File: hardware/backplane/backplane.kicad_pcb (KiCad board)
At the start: 4 copper layers, 123.4 x 458 mm, 31 parts, among them J1 Conn_02x34_Odd_Even, J101 Conn_02x34_Odd_Even, J102 ERF8-060-05.0-L-DV, J103 Conn_02x34_Odd_Even, J2 ERF8-060-05.0-L-DV, J201 Conn_02x34_Odd_Even-Connector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, J203 Conn_02x34_Odd_Even-Connector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, J3 Conn_02x34_Odd_Even, J301 Conn_02x34_Odd_Even-Connector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, J302 ERF8-060-05.0-L-DV, J303 Conn_02x34_Odd_Even-Connector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, J401 Conn_02x34_Odd_Even, J402 ERF8-060-05.0-L-DV, J403 Conn_02x34_Odd_Even, J501 Conn_02x34_Odd_Even-Connector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, J503 Conn_02x34_Odd_Even-Connector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, J601 Conn_02x34_Odd_Even-Connector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, J602 ERF8-060-05.0-L-DV, J603 Conn_02x34_Odd_Even-Connector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, J701 Conn_02x34_Odd_Even, J702 ERF8-060-05.0-L-DV, J703 Conn_02x34_Odd_Even, J801 Conn_02x34_Odd_Even-Connector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, J803 Conn_02x34_Odd_Even-Connector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, J901 Conn_02x34_Odd_Even-Connector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, J902 ERF8-060-05.0-L-DV, J903 Conn_02x34_Odd_Even-Connector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

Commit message: Backplane Layout in process
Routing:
- net GND: track 118.4 -> 530.2 mm, vias 42 -> 185
- net /SiPM_Connector(1-3)/BIAS1: track 0.00 -> 275.8 mm, vias 0 -> 5
- net /SiPM_Connector(1-3)/BIAS2: track 0.00 -> 111.6 mm, vias 0 -> 5
- net /SiPM_Connector(1-3)/OUT: track 0.00 -> 57.8 mm, vias 0 -> 3
- net /SiPM_Connector(1-3)/VDD: track 0.00 -> 54.1 mm, vias 0 -> 3
- net /SiPM_Connector(1-3)/BIAS3: track 0.00 -> 46.7 mm, vias 0 -> 1
- net /SiPM_Connector(1-3)/CH46: track 0.00 -> 40.6 mm, vias 0 -> 4
- net /SiPM_Connector(1-3)/CH45: track 0.00 -> 39.9 mm, vias 0 -> 2
- net /SiPM_Connector(1-3)/CH47: track 0.00 -> 39.7 mm, vias 0 -> 2
- net /SiPM_Connector(1-3)/CH53: track 0.00 -> 39.5 mm, vias 0 -> 2
- net /SiPM_Connector(1-3)/CH56: track 0.00 -> 39.4 mm, vias 0 -> 2
- net /SiPM_Connector(1-3)/CH52: track 0.00 -> 39.3 mm, vias 0 -> 4
- net /SiPM_Connector(1-3)/CH55: track 0.00 -> 39.2 mm, vias 0 -> 4
- net /SiPM_Connector(1-3)/CH54: track 0.00 -> 39.1 mm, vias 0 -> 2
- net /SiPM_Connector(1-3)/CH44: track 0.00 -> 39.0 mm, vias 0 -> 2
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
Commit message: Backplane layout in process
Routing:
- net /SiPM_Connector(1-3)/BIAS1: track 275.8 -> 161.3 mm, vias 5 -> 3
- net /SiPM_Connector(1-3)/BIAS3: track 46.7 -> 161.3 mm, vias 1 -> 3
- net GND: track 530.2 -> 476.0 mm, vias 185 -> 168
- net /SiPM_Connector(1-3)/BIAS4: track 15.9 -> 63.8 mm, vias 1 -> 3
- net /SiPM_Connector(1-3)/BIAS2: track 111.6 -> 63.8 mm, vias 5 -> 3
- net /SiPM_Connector(1-3)/BCH46: track 0.00 -> 20.3 mm, vias 0 -> 2
- net /SiPM_Connector(1-3)/CH46: track 40.6 -> 20.3 mm, vias 4 -> 2
- net /SiPM_Connector(1-3)/BCH45: track 0.00 -> 20.0 mm, vias 0 -> 1
- net /SiPM_Connector(1-3)/CH45: track 39.9 -> 20.0 mm, vias 2 -> 1
- net /SiPM_Connector(1-3)/CH47: track 39.7 -> 19.8 mm, vias 2 -> 1
- net /SiPM_Connector(1-3)/BCH47: track 0.00 -> 19.8 mm, vias 0 -> 1
- net /SiPM_Connector(1-3)/BCH53: track 0.00 -> 19.7 mm, vias 0 -> 1
- net /SiPM_Connector(1-3)/CH53: track 39.5 -> 19.7 mm, vias 2 -> 1
- net /SiPM_Connector(1-3)/BCH56: track 0.00 -> 19.7 mm, vias 0 -> 1
- net /SiPM_Connector(1-3)/CH56: track 39.4 -> 19.7 mm, vias 2 -> 1
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
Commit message: SiPM Board RevC layout modified
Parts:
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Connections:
- J103 pad 1: Net-(J103-Pad1) -> /SiPM_Connector(1-3)/BIAS3
- J103 pad 10: GND -> /SiPM_Connector(1-3)/BCH4
- J103 pad 11: /SiPM_Connector(1-3)/BCH28 -> GND
- J103 pad 12: GND -> /SiPM_Connector(1-3)/BCH5
- J103 pad 13: /SiPM_Connector(1-3)/BCH27 -> GND
- J103 pad 14: GND -> /SiPM_Connector(1-3)/BCH6
- J103 pad 15: /SiPM_Connector(1-3)/BCH26 -> GND
- J103 pad 16: GND -> /SiPM_Connector(1-3)/BCH7
- J103 pad 17: /SiPM_Connector(1-3)/BCH25 -> GND
- J103 pad 18: GND -> /SiPM_Connector(1-3)/BCH8
- J103 pad 19: /SiPM_Connector(1-3)/BCH24 -> GND
- J103 pad 2: /SiPM_Connector(1-3)/BIAS4 -> /SiPM_Connector(1-3)/BCH0
- J103 pad 20: GND -> /SiPM_Connector(1-3)/BCH9
- J103 pad 21: /SiPM_Connector(1-3)/BCH23 -> GND
- J103 pad 22: GND -> /SiPM_Connector(1-3)/BCH10
- J103 pad 23: /SiPM_Connector(1-3)/BCH22 -> GND
- J103 pad 24: GND -> /SiPM_Connector(1-3)/BCH11
- J103 pad 25: /SiPM_Connector(1-3)/BCH21 -> GND
- J103 pad 26: GND -> /SiPM_Connector(1-3)/BCH12
- J103 pad 27: /SiPM_Connector(1-3)/BCH20 -> GND
- J103 pad 28: GND -> /SiPM_Connector(1-3)/BCH13
- J103 pad 29: /SiPM_Connector(1-3)/BCH19 -> GND
- J103 pad 3: Net-(J103-Pad3) -> GND
- J103 pad 30: GND -> /SiPM_Connector(1-3)/BCH14
- J103 pad 31: /SiPM_Connector(1-3)/BCH18 -> GND
- J103 pad 32: GND -> /SiPM_Connector(1-3)/BCH15
- J103 pad 33: /SiPM_Connector(1-3)/BCH17 -> GND
- J103 pad 34: GND -> /SiPM_Connector(1-3)/BCH16
- J103 pad 35: /SiPM_Connector(1-3)/BCH16 -> GND
- J103 pad 36: GND -> /SiPM_Connector(1-3)/BCH17
- J103 pad 37: /SiPM_Connector(1-3)/BCH15 -> GND
- J103 pad 38: GND -> /SiPM_Connector(1-3)/BCH18
- J103 pad 39: /SiPM_Connector(1-3)/BCH14 -> GND
- J103 pad 4: GND -> /SiPM_Connector(1-3)/BCH1
- J103 pad 40: GND -> /SiPM_Connector(1-3)/BCH19
- J103 pad 41: /SiPM_Connector(1-3)/BCH13 -> GND
- J103 pad 42: GND -> /SiPM_Connector(1-3)/BCH20
- J103 pad 43: /SiPM_Connector(1-3)/BCH12 -> GND
- J103 pad 44: GND -> /SiPM_Connector(1-3)/BCH21
- J103 pad 45: /SiPM_Connector(1-3)/BCH11 -> GND
- J103 pad 46: GND -> /SiPM_Connector(1-3)/BCH22
- J103 pad 47: /SiPM_Connector(1-3)/BCH10 -> GND
- J103 pad 48: GND -> /SiPM_Connector(1-3)/BCH23
- J103 pad 49: /SiPM_Connector(1-3)/BCH9 -> GND
- J103 pad 5: /SiPM_Connector(1-3)/BCH31 -> GND
- J103 pad 50: GND -> /SiPM_Connector(1-3)/BCH24
- J103 pad 51: /SiPM_Connector(1-3)/BCH8 -> GND
- J103 pad 52: GND -> /SiPM_Connector(1-3)/BCH25
- J103 pad 53: /SiPM_Connector(1-3)/BCH7 -> GND
- J103 pad 54: GND -> /SiPM_Connector(1-3)/BCH26
- J103 pad 55: /SiPM_Connector(1-3)/BCH6 -> GND
- J103 pad 56: GND -> /SiPM_Connector(1-3)/BCH27
- J103 pad 57: /SiPM_Connector(1-3)/BCH5 -> GND
- J103 pad 58: GND -> /SiPM_Connector(1-3)/BCH28
- J103 pad 59: /SiPM_Connector(1-3)/BCH4 -> GND
- J103 pad 6: GND -> /SiPM_Connector(1-3)/BCH2
- J103 pad 60: GND -> /SiPM_Connector(1-3)/BCH29
- J103 pad 61: /SiPM_Connector(1-3)/BCH3 -> GND
- J103 pad 62: GND -> /SiPM_Connector(1-3)/BCH30
- J103 pad 63: /SiPM_Connector(1-3)/BCH2 -> GND
- J103 pad 64: GND -> /SiPM_Connector(1-3)/BCH31
- J103 pad 65: /SiPM_Connector(1-3)/BCH1 -> GND
- J103 pad 66: GND -> Net-(J103-Pad66)
- J103 pad 67: /SiPM_Connector(1-3)/BCH0 -> /SiPM_Connector(1-3)/BIAS4
- J103 pad 68: /SiPM_Connector(1-3)/BIAS3 -> Net-(J103-Pad68)
- J103 pad 7: /SiPM_Connector(1-3)/BCH30 -> GND
- J103 pad 8: GND -> /SiPM_Connector(1-3)/BCH3
- J103 pad 9: /SiPM_Connector(1-3)/BCH29 -> GND
- J203 pad 1: Net-(J203-Pad1) -> /SiPM_Connector(1-3)/BIAS3
- J203 pad 10: GND -> /SiPM_Connector(1-3)/BCH36
- J203 pad 11: /SiPM_Connector(1-3)/BCH60 -> GND
- J203 pad 12: GND -> /SiPM_Connector(1-3)/BCH37
- J203 pad 13: /SiPM_Connector(1-3)/BCH59 -> GND
- J203 pad 14: GND -> /SiPM_Connector(1-3)/BCH38
- J203 pad 15: /SiPM_Connector(1-3)/BCH58 -> GND
- J203 pad 16: GND -> /SiPM_Connector(1-3)/BCH39
- J203 pad 17: /SiPM_Connector(1-3)/BCH57 -> GND
- J203 pad 18: GND -> /SiPM_Connector(1-3)/BCH40
- J203 pad 19: /SiPM_Connector(1-3)/BCH56 -> GND
- J203 pad 2: /SiPM_Connector(1-3)/BIAS4 -> /SiPM_Connector(1-3)/BCH32
- J203 pad 20: GND -> /SiPM_Connector(1-3)/BCH41
- J203 pad 21: /SiPM_Connector(1-3)/BCH55 -> GND
- J203 pad 22: GND -> /SiPM_Connector(1-3)/BCH42
- J203 pad 23: /SiPM_Connector(1-3)/BCH54 -> GND
- J203 pad 24: GND -> /SiPM_Connector(1-3)/BCH43
- J203 pad 25: /SiPM_Connector(1-3)/BCH53 -> GND
- J203 pad 26: GND -> /SiPM_Connector(1-3)/BCH44
- J203 pad 27: /SiPM_Connector(1-3)/BCH52 -> GND
- J203 pad 28: GND -> /SiPM_Connector(1-3)/BCH45
- J203 pad 29: /SiPM_Connector(1-3)/BCH51 -> GND
- J203 pad 3: Net-(J203-Pad3) -> GND
- J203 pad 30: GND -> /SiPM_Connector(1-3)/BCH46
- J203 pad 31: /SiPM_Connector(1-3)/BCH50 -> GND
- J203 pad 32: GND -> /SiPM_Connector(1-3)/BCH47
- J203 pad 33: /SiPM_Connector(1-3)/BCH49 -> GND
- J203 pad 34: GND -> /SiPM_Connector(1-3)/BCH48
- J203 pad 35: /SiPM_Connector(1-3)/BCH48 -> GND
- J203 pad 36: GND -> /SiPM_Connector(1-3)/BCH49
- J203 pad 37: /SiPM_Connector(1-3)/BCH47 -> GND
- J203 pad 38: GND -> /SiPM_Connector(1-3)/BCH50
- J203 pad 39: /SiPM_Connector(1-3)/BCH46 -> GND
- J203 pad 4: GND -> /SiPM_Connector(1-3)/BCH33
- J203 pad 40: GND -> /SiPM_Connector(1-3)/BCH51
- J203 pad 41: /SiPM_Connector(1-3)/BCH45 -> GND
- J203 pad 42: GND -> /SiPM_Connector(1-3)/BCH52
- J203 pad 43: /SiPM_Connector(1-3)/BCH44 -> GND
- J203 pad 44: GND -> /SiPM_Connector(1-3)/BCH53
- J203 pad 45: /SiPM_Connector(1-3)/BCH43 -> GND
- J203 pad 46: GND -> /SiPM_Connector(1-3)/BCH54
- J203 pad 47: /SiPM_Connector(1-3)/BCH42 -> GND
- J203 pad 48: GND -> /SiPM_Connector(1-3)/BCH55
- J203 pad 49: /SiPM_Connector(1-3)/BCH41 -> GND
- J203 pad 5: /SiPM_Connector(1-3)/BCH63 -> GND
- J203 pad 50: GND -> /SiPM_Connector(1-3)/BCH56
- J203 pad 51: /SiPM_Connector(1-3)/BCH40 -> GND
- J203 pad 52: GND -> /SiPM_Connector(1-3)/BCH57
- J203 pad 53: /SiPM_Connector(1-3)/BCH39 -> GND
- J203 pad 54: GND -> /SiPM_Connector(1-3)/BCH58
- J203 pad 55: /SiPM_Connector(1-3)/BCH38 -> GND
- J203 pad 56: GND -> /SiPM_Connector(1-3)/BCH59
- J203 pad 57: /SiPM_Connector(1-3)/BCH37 -> GND
- J203 pad 58: GND -> /SiPM_Connector(1-3)/BCH60
- J203 pad 59: /SiPM_Connector(1-3)/BCH36 -> GND
- J203 pad 6: GND -> /SiPM_Connector(1-3)/BCH34
- J203 pad 60: GND -> /SiPM_Connector(1-3)/BCH61
- J203 pad 61: /SiPM_Connector(1-3)/BCH35 -> GND
- J203 pad 62: GND -> /SiPM_Connector(1-3)/BCH62
- J203 pad 63: /SiPM_Connector(1-3)/BCH34 -> GND
- J203 pad 64: GND -> /SiPM_Connector(1-3)/BCH63
- J203 pad 65: /SiPM_Connector(1-3)/BCH33 -> GND
- J203 pad 66: GND -> Net-(J203-Pad66)
- J203 pad 67: /SiPM_Connector(1-3)/BCH32 -> /SiPM_Connector(1-3)/BIAS4
- J203 pad 68: /SiPM_Connector(1-3)/BIAS3 -> Net-(J203-Pad68)
- J203 pad 7: /SiPM_Connector(1-3)/BCH62 -> GND
- J203 pad 8: GND -> /SiPM_Connector(1-3)/BCH35
- J203 pad 9: /SiPM_Connector(1-3)/BCH61 -> GND
- J303 pad 1: Net-(J303-Pad1) -> /SiPM_Connector(1-3)/BIAS3
- J303 pad 10: GND -> /SiPM_Connector(1-3)/BCH68
- J303 pad 11: /SiPM_Connector(1-3)/BCH92 -> GND
- J303 pad 12: GND -> /SiPM_Connector(1-3)/BCH69
- J303 pad 13: /SiPM_Connector(1-3)/BCH91 -> GND
- J303 pad 14: GND -> /SiPM_Connector(1-3)/BCH70
- J303 pad 15: /SiPM_Connector(1-3)/BCH90 -> GND
- J303 pad 16: GND -> /SiPM_Connector(1-3)/BCH71
- J303 pad 17: /SiPM_Connector(1-3)/BCH89 -> GND
- J303 pad 18: GND -> /SiPM_Connector(1-3)/BCH72
- J303 pad 19: /SiPM_Connector(1-3)/BCH88 -> GND
- J303 pad 2: /SiPM_Connector(1-3)/BIAS4 -> /SiPM_Connector(1-3)/BCH64
- J303 pad 20: GND -> /SiPM_Connector(1-3)/BCH73
- J303 pad 21: /SiPM_Connector(1-3)/BCH87 -> GND
- J303 pad 22: GND -> /SiPM_Connector(1-3)/BCH74
- J303 pad 23: /SiPM_Connector(1-3)/BCH86 -> GND
- J303 pad 24: GND -> /SiPM_Connector(1-3)/BCH75
- J303 pad 25: /SiPM_Connector(1-3)/BCH85 -> GND
- J303 pad 26: GND -> /SiPM_Connector(1-3)/BCH76
- J303 pad 27: /SiPM_Connector(1-3)/BCH84 -> GND
- J303 pad 28: GND -> /SiPM_Connector(1-3)/BCH77
- J303 pad 29: /SiPM_Connector(1-3)/BCH83 -> GND
- J303 pad 3: Net-(J303-Pad3) -> GND
- J303 pad 30: GND -> /SiPM_Connector(1-3)/BCH78
- J303 pad 31: /SiPM_Connector(1-3)/BCH82 -> GND
- J303 pad 32: GND -> /SiPM_Connector(1-3)/BCH79
- J303 pad 33: /SiPM_Connector(1-3)/BCH81 -> GND
- J303 pad 34: GND -> /SiPM_Connector(1-3)/BCH80
- J303 pad 35: /SiPM_Connector(1-3)/BCH80 -> GND
- J303 pad 36: GND -> /SiPM_Connector(1-3)/BCH81
- J303 pad 37: /SiPM_Connector(1-3)/BCH79 -> GND
- J303 pad 38: GND -> /SiPM_Connector(1-3)/BCH82
- J303 pad 39: /SiPM_Connector(1-3)/BCH78 -> GND
- J303 pad 4: GND -> /SiPM_Connector(1-3)/BCH65
- J303 pad 40: GND -> /SiPM_Connector(1-3)/BCH83
- J303 pad 41: /SiPM_Connector(1-3)/BCH77 -> GND
- J303 pad 42: GND -> /SiPM_Connector(1-3)/BCH84
- J303 pad 43: /SiPM_Connector(1-3)/BCH76 -> GND
- J303 pad 44: GND -> /SiPM_Connector(1-3)/BCH85
- J303 pad 45: /SiPM_Connector(1-3)/BCH75 -> GND
- J303 pad 46: GND -> /SiPM_Connector(1-3)/BCH86
- J303 pad 47: /SiPM_Connector(1-3)/BCH74 -> GND
- J303 pad 48: GND -> /SiPM_Connector(1-3)/BCH87
- J303 pad 49: /SiPM_Connector(1-3)/BCH73 -> GND
- J303 pad 5: /SiPM_Connector(1-3)/BCH95 -> GND
- J303 pad 50: GND -> /SiPM_Connector(1-3)/BCH88
- J303 pad 51: /SiPM_Connector(1-3)/BCH72 -> GND
- J303 pad 52: GND -> /SiPM_Connector(1-3)/BCH89
- J303 pad 53: /SiPM_Connector(1-3)/BCH71 -> GND
- J303 pad 54: GND -> /SiPM_Connector(1-3)/BCH90
- J303 pad 55: /SiPM_Connector(1-3)/BCH70 -> GND
- J303 pad 56: GND -> /SiPM_Connector(1-3)/BCH91
- J303 pad 57: /SiPM_Connector(1-3)/BCH69 -> GND
- J303 pad 58: GND -> /SiPM_Connector(1-3)/BCH92
- J303 pad 59: /SiPM_Connector(1-3)/BCH68 -> GND
- J303 pad 6: GND -> /SiPM_Connector(1-3)/BCH66
- J303 pad 60: GND -> /SiPM_Connector(1-3)/BCH93
- J303 pad 61: /SiPM_Connector(1-3)/BCH67 -> GND
- J303 pad 62: GND -> /SiPM_Connector(1-3)/BCH94
- J303 pad 63: /SiPM_Connector(1-3)/BCH66 -> GND
- J303 pad 64: GND -> /SiPM_Connector(1-3)/BCH95
- J303 pad 65: /SiPM_Connector(1-3)/BCH65 -> GND
- J303 pad 66: GND -> Net-(J303-Pad66)
- J303 pad 67: /SiPM_Connector(1-3)/BCH64 -> /SiPM_Connector(1-3)/BIAS4
- J303 pad 68: /SiPM_Connector(1-3)/BIAS3 -> Net-(J303-Pad68)
- J303 pad 7: /SiPM_Connector(1-3)/BCH94 -> GND
- J303 pad 8: GND -> /SiPM_Connector(1-3)/BCH67
- J303 pad 9: /SiPM_Connector(1-3)/BCH93 -> GND
- J403 pad 1: Net-(J403-Pad1) -> /SiPM_Connector(4-6)/BIAS3
- J403 pad 10: GND -> /SiPM_Connector(4-6)/BCH4
- J403 pad 11: /SiPM_Connector(4-6)/BCH28 -> GND
- J403 pad 12: GND -> /SiPM_Connector(4-6)/BCH5
- J403 pad 13: /SiPM_Connector(4-6)/BCH27 -> GND
- J403 pad 14: GND -> /SiPM_Connector(4-6)/BCH6
- J403 pad 15: /SiPM_Connector(4-6)/BCH26 -> GND
- J403 pad 16: GND -> /SiPM_Connector(4-6)/BCH7
- J403 pad 17: /SiPM_Connector(4-6)/BCH25 -> GND
- J403 pad 18: GND -> /SiPM_Connector(4-6)/BCH8
- J403 pad 19: /SiPM_Connector(4-6)/BCH24 -> GND
- J403 pad 2: /SiPM_Connector(4-6)/BIAS4 -> /SiPM_Connector(4-6)/BCH0
- J403 pad 20: GND -> /SiPM_Connector(4-6)/BCH9
- J403 pad 21: /SiPM_Connector(4-6)/BCH23 -> GND
- J403 pad 22: GND -> /SiPM_Connector(4-6)/BCH10
- J403 pad 23: /SiPM_Connector(4-6)/BCH22 -> GND
- J403 pad 24: GND -> /SiPM_Connector(4-6)/BCH11
- J403 pad 25: /SiPM_Connector(4-6)/BCH21 -> GND
- J403 pad 26: GND -> /SiPM_Connector(4-6)/BCH12
- J403 pad 27: /SiPM_Connector(4-6)/BCH20 -> GND
- J403 pad 28: GND -> /SiPM_Connector(4-6)/BCH13
- J403 pad 29: /SiPM_Connector(4-6)/BCH19 -> GND
- J403 pad 3: Net-(J403-Pad3) -> GND
- J403 pad 30: GND -> /SiPM_Connector(4-6)/BCH14
- J403 pad 31: /SiPM_Connector(4-6)/BCH18 -> GND
- J403 pad 32: GND -> /SiPM_Connector(4-6)/BCH15
- J403 pad 33: /SiPM_Connector(4-6)/BCH17 -> GND
- J403 pad 34: GND -> /SiPM_Connector(4-6)/BCH16
- J403 pad 35: /SiPM_Connector(4-6)/BCH16 -> GND
- J403 pad 36: GND -> /SiPM_Connector(4-6)/BCH17
- J403 pad 37: /SiPM_Connector(4-6)/BCH15 -> GND
- J403 pad 38: GND -> /SiPM_Connector(4-6)/BCH18
- J403 pad 39: /SiPM_Connector(4-6)/BCH14 -> GND
- J403 pad 4: GND -> /SiPM_Connector(4-6)/BCH1
- J403 pad 40: GND -> /SiPM_Connector(4-6)/BCH19
- J403 pad 41: /SiPM_Connector(4-6)/BCH13 -> GND
- J403 pad 42: GND -> /SiPM_Connector(4-6)/BCH20
- J403 pad 43: /SiPM_Connector(4-6)/BCH12 -> GND
- J403 pad 44: GND -> /SiPM_Connector(4-6)/BCH21
- J403 pad 45: /SiPM_Connector(4-6)/BCH11 -> GND
- J403 pad 46: GND -> /SiPM_Connector(4-6)/BCH22
- J403 pad 47: /SiPM_Connector(4-6)/BCH10 -> GND
- J403 pad 48: GND -> /SiPM_Connector(4-6)/BCH23
- J403 pad 49: /SiPM_Connector(4-6)/BCH9 -> GND
- J403 pad 5: /SiPM_Connector(4-6)/BCH31 -> GND
- J403 pad 50: GND -> /SiPM_Connector(4-6)/BCH24
- J403 pad 51: /SiPM_Connector(4-6)/BCH8 -> GND
- J403 pad 52: GND -> /SiPM_Connector(4-6)/BCH25
- J403 pad 53: /SiPM_Connector(4-6)/BCH7 -> GND
- J403 pad 54: GND -> /SiPM_Connector(4-6)/BCH26
- J403 pad 55: /SiPM_Connector(4-6)/BCH6 -> GND
- J403 pad 56: GND -> /SiPM_Connector(4-6)/BCH27
- J403 pad 57: /SiPM_Connector(4-6)/BCH5 -> GND
- J403 pad 58: GND -> /SiPM_Connector(4-6)/BCH28
- J403 pad 59: /SiPM_Connector(4-6)/BCH4 -> GND
- J403 pad 6: GND -> /SiPM_Connector(4-6)/BCH2
- J403 pad 60: GND -> /SiPM_Connector(4-6)/BCH29
- J403 pad 61: /SiPM_Connector(4-6)/BCH3 -> GND
- J403 pad 62: GND -> /SiPM_Connector(4-6)/BCH30
- J403 pad 63: /SiPM_Connector(4-6)/BCH2 -> GND
- J403 pad 64: GND -> /SiPM_Connector(4-6)/BCH31
- J403 pad 65: /SiPM_Connector(4-6)/BCH1 -> GND
- J403 pad 66: GND -> Net-(J403-Pad66)
- J403 pad 67: /SiPM_Connector(4-6)/BCH0 -> /SiPM_Connector(4-6)/BIAS4
- J403 pad 68: /SiPM_Connector(4-6)/BIAS3 -> Net-(J403-Pad68)
- J403 pad 7: /SiPM_Connector(4-6)/BCH30 -> GND
- J403 pad 8: GND -> /SiPM_Connector(4-6)/BCH3
- J403 pad 9: /SiPM_Connector(4-6)/BCH29 -> GND
- J503 pad 1: Net-(J503-Pad1) -> /SiPM_Connector(4-6)/BIAS3
- J503 pad 10: GND -> /SiPM_Connector(4-6)/BCH36
- J503 pad 11: /SiPM_Connector(4-6)/BCH60 -> GND
- J503 pad 12: GND -> /SiPM_Connector(4-6)/BCH37
- J503 pad 13: /SiPM_Connector(4-6)/BCH59 -> GND
- J503 pad 14: GND -> /SiPM_Connector(4-6)/BCH38
- J503 pad 15: /SiPM_Connector(4-6)/BCH58 -> GND
- J503 pad 16: GND -> /SiPM_Connector(4-6)/BCH39
- J503 pad 17: /SiPM_Connector(4-6)/BCH57 -> GND
- J503 pad 18: GND -> /SiPM_Connector(4-6)/BCH40
- J503 pad 19: /SiPM_Connector(4-6)/BCH56 -> GND
- J503 pad 2: /SiPM_Connector(4-6)/BIAS4 -> /SiPM_Connector(4-6)/BCH32
- J503 pad 20: GND -> /SiPM_Connector(4-6)/BCH41
- J503 pad 21: /SiPM_Connector(4-6)/BCH55 -> GND
- J503 pad 22: GND -> /SiPM_Connector(4-6)/BCH42
- J503 pad 23: /SiPM_Connector(4-6)/BCH54 -> GND
- J503 pad 24: GND -> /SiPM_Connector(4-6)/BCH43
- J503 pad 25: /SiPM_Connector(4-6)/BCH53 -> GND
- J503 pad 26: GND -> /SiPM_Connector(4-6)/BCH44
- J503 pad 27: /SiPM_Connector(4-6)/BCH52 -> GND
- J503 pad 28: GND -> /SiPM_Connector(4-6)/BCH45
- J503 pad 29: /SiPM_Connector(4-6)/BCH51 -> GND
- J503 pad 3: Net-(J503-Pad3) -> GND
- J503 pad 30: GND -> /SiPM_Connector(4-6)/BCH46
- J503 pad 31: /SiPM_Connector(4-6)/BCH50 -> GND
- J503 pad 32: GND -> /SiPM_Connector(4-6)/BCH47
- J503 pad 33: /SiPM_Connector(4-6)/BCH49 -> GND
- J503 pad 34: GND -> /SiPM_Connector(4-6)/BCH48
- J503 pad 35: /SiPM_Connector(4-6)/BCH48 -> GND
- J503 pad 36: GND -> /SiPM_Connector(4-6)/BCH49
- J503 pad 37: /SiPM_Connector(4-6)/BCH47 -> GND
- J503 pad 38: GND -> /SiPM_Connector(4-6)/BCH50
- J503 pad 39: /SiPM_Connector(4-6)/BCH46 -> GND
- J503 pad 4: GND -> /SiPM_Connector(4-6)/BCH33
- J503 pad 40: GND -> /SiPM_Connector(4-6)/BCH51
- J503 pad 41: /SiPM_Connector(4-6)/BCH45 -> GND
- J503 pad 42: GND -> /SiPM_Connector(4-6)/BCH52
- J503 pad 43: /SiPM_Connector(4-6)/BCH44 -> GND
- J503 pad 44: GND -> /SiPM_Connector(4-6)/BCH53
- J503 pad 45: /SiPM_Connector(4-6)/BCH43 -> GND
- J503 pad 46: GND -> /SiPM_Connector(4-6)/BCH54
- J503 pad 47: /SiPM_Connector(4-6)/BCH42 -> GND
- J503 pad 48: GND -> /SiPM_Connector(4-6)/BCH55
- J503 pad 49: /SiPM_Connector(4-6)/BCH41 -> GND
- J503 pad 5: /SiPM_Connector(4-6)/BCH63 -> GND
- J503 pad 50: GND -> /SiPM_Connector(4-6)/BCH56
- J503 pad 51: /SiPM_Connector(4-6)/BCH40 -> GND
- J503 pad 52: GND -> /SiPM_Connector(4-6)/BCH57
- J503 pad 53: /SiPM_Connector(4-6)/BCH39 -> GND
- J503 pad 54: GND -> /SiPM_Connector(4-6)/BCH58
- J503 pad 55: /SiPM_Connector(4-6)/BCH38 -> GND
- J503 pad 56: GND -> /SiPM_Connector(4-6)/BCH59
- J503 pad 57: /SiPM_Connector(4-6)/BCH37 -> GND
- J503 pad 58: GND -> /SiPM_Connector(4-6)/BCH60
- J503 pad 59: /SiPM_Connector(4-6)/BCH36 -> GND
- J503 pad 6: GND -> /SiPM_Connector(4-6)/BCH34
- J503 pad 60: GND -> /SiPM_Connector(4-6)/BCH61
- J503 pad 61: /SiPM_Connector(4-6)/BCH35 -> GND
- J503 pad 62: GND -> /SiPM_Connector(4-6)/BCH62
- J503 pad 63: /SiPM_Connector(4-6)/BCH34 -> GND
- J503 pad 64: GND -> /SiPM_Connector(4-6)/BCH63
- J503 pad 65: /SiPM_Connector(4-6)/BCH33 -> GND
- J503 pad 66: GND -> Net-(J503-Pad66)
- J503 pad 67: /SiPM_Connector(4-6)/BCH32 -> /SiPM_Connector(4-6)/BIAS4
- J503 pad 68: /SiPM_Connector(4-6)/BIAS3 -> Net-(J503-Pad68)
- J503 pad 7: /SiPM_Connector(4-6)/BCH62 -> GND
- J503 pad 8: GND -> /SiPM_Connector(4-6)/BCH35
- J503 pad 9: /SiPM_Connector(4-6)/BCH61 -> GND
- J603 pad 1: Net-(J603-Pad1) -> /SiPM_Connector(4-6)/BIAS3
- J603 pad 10: GND -> /SiPM_Connector(4-6)/BCH68
- J603 pad 11: /SiPM_Connector(4-6)/BCH92 -> GND
- J603 pad 12: GND -> /SiPM_Connector(4-6)/BCH69
- J603 pad 13: /SiPM_Connector(4-6)/BCH91 -> GND
- J603 pad 14: GND -> /SiPM_Connector(4-6)/BCH70
- J603 pad 15: /SiPM_Connector(4-6)/BCH90 -> GND
- J603 pad 16: GND -> /SiPM_Connector(4-6)/BCH71
- J603 pad 17: /SiPM_Connector(4-6)/BCH89 -> GND
- J603 pad 18: GND -> /SiPM_Connector(4-6)/BCH72
- J603 pad 19: /SiPM_Connector(4-6)/BCH88 -> GND
- J603 pad 2: /SiPM_Connector(4-6)/BIAS4 -> /SiPM_Connector(4-6)/BCH64
- J603 pad 20: GND -> /SiPM_Connector(4-6)/BCH73
- J603 pad 21: /SiPM_Connector(4-6)/BCH87 -> GND
- J603 pad 22: GND -> /SiPM_Connector(4-6)/BCH74
- J603 pad 23: /SiPM_Connector(4-6)/BCH86 -> GND
- J603 pad 24: GND -> /SiPM_Connector(4-6)/BCH75
- J603 pad 25: /SiPM_Connector(4-6)/BCH85 -> GND
- J603 pad 26: GND -> /SiPM_Connector(4-6)/BCH76
- J603 pad 27: /SiPM_Connector(4-6)/BCH84 -> GND
- J603 pad 28: GND -> /SiPM_Connector(4-6)/BCH77
- J603 pad 29: /SiPM_Connector(4-6)/BCH83 -> GND
- J603 pad 3: Net-(J603-Pad3) -> GND
- J603 pad 30: GND -> /SiPM_Connector(4-6)/BCH78
- J603 pad 31: /SiPM_Connector(4-6)/BCH82 -> GND
- J603 pad 32: GND -> /SiPM_Connector(4-6)/BCH79
- J603 pad 33: /SiPM_Connector(4-6)/BCH81 -> GND
- J603 pad 34: GND -> /SiPM_Connector(4-6)/BCH80
- J603 pad 35: /SiPM_Connector(4-6)/BCH80 -> GND
- J603 pad 36: GND -> /SiPM_Connector(4-6)/BCH81
- J603 pad 37: /SiPM_Connector(4-6)/BCH79 -> GND
- J603 pad 38: GND -> /SiPM_Connector(4-6)/BCH82
- J603 pad 39: /SiPM_Connector(4-6)/BCH78 -> GND
- J603 pad 4: GND -> /SiPM_Connector(4-6)/BCH65
- J603 pad 40: GND -> /SiPM_Connector(4-6)/BCH83
- J603 pad 41: /SiPM_Connector(4-6)/BCH77 -> GND
- J603 pad 42: GND -> /SiPM_Connector(4-6)/BCH84
- J603 pad 43: /SiPM_Connector(4-6)/BCH76 -> GND
- J603 pad 44: GND -> /SiPM_Connector(4-6)/BCH85
- J603 pad 45: /SiPM_Connector(4-6)/BCH75 -> GND
- J603 pad 46: GND -> /SiPM_Connector(4-6)/BCH86
- J603 pad 47: /SiPM_Connector(4-6)/BCH74 -> GND
- J603 pad 48: GND -> /SiPM_Connector(4-6)/BCH87
- J603 pad 49: /SiPM_Connector(4-6)/BCH73 -> GND
- J603 pad 5: /SiPM_Connector(4-6)/BCH95 -> GND
- J603 pad 50: GND -> /SiPM_Connector(4-6)/BCH88
- J603 pad 51: /SiPM_Connector(4-6)/BCH72 -> GND
- J603 pad 52: GND -> /SiPM_Connector(4-6)/BCH89
- J603 pad 53: /SiPM_Connector(4-6)/BCH71 -> GND
- J603 pad 54: GND -> /SiPM_Connector(4-6)/BCH90
- J603 pad 55: /SiPM_Connector(4-6)/BCH70 -> GND
- J603 pad 56: GND -> /SiPM_Connector(4-6)/BCH91
- J603 pad 57: /SiPM_Connector(4-6)/BCH69 -> GND
- J603 pad 58: GND -> /SiPM_Connector(4-6)/BCH92
- J603 pad 59: /SiPM_Connector(4-6)/BCH68 -> GND
- J603 pad 6: GND -> /SiPM_Connector(4-6)/BCH66
- J603 pad 60: GND -> /SiPM_Connector(4-6)/BCH93
- J603 pad 61: /SiPM_Connector(4-6)/BCH67 -> GND
- J603 pad 62: GND -> /SiPM_Connector(4-6)/BCH94
- J603 pad 63: /SiPM_Connector(4-6)/BCH66 -> GND
- J603 pad 64: GND -> /SiPM_Connector(4-6)/BCH95
- J603 pad 65: /SiPM_Connector(4-6)/BCH65 -> GND
- J603 pad 66: GND -> Net-(J603-Pad66)
- J603 pad 67: /SiPM_Connector(4-6)/BCH64 -> /SiPM_Connector(4-6)/BIAS4
- J603 pad 68: /SiPM_Connector(4-6)/BIAS3 -> Net-(J603-Pad68)
- J603 pad 7: /SiPM_Connector(4-6)/BCH94 -> GND
- J603 pad 8: GND -> /SiPM_Connector(4-6)/BCH67
- J603 pad 9: /SiPM_Connector(4-6)/BCH93 -> GND
- J703 pad 1: Net-(J703-Pad1) -> /SiPM_Connector(7-9)/BIAS3
- J703 pad 10: GND -> /SiPM_Connector(7-9)/BCH4
- J703 pad 11: /SiPM_Connector(7-9)/BCH28 -> GND
- J703 pad 12: GND -> /SiPM_Connector(7-9)/BCH5
- J703 pad 13: /SiPM_Connector(7-9)/BCH27 -> GND
- J703 pad 14: GND -> /SiPM_Connector(7-9)/BCH6
- J703 pad 15: /SiPM_Connector(7-9)/BCH26 -> GND
- J703 pad 16: GND -> /SiPM_Connector(7-9)/BCH7
- J703 pad 17: /SiPM_Connector(7-9)/BCH25 -> GND
- J703 pad 18: GND -> /SiPM_Connector(7-9)/BCH8
- J703 pad 19: /SiPM_Connector(7-9)/BCH24 -> GND
- J703 pad 2: /SiPM_Connector(7-9)/BIAS4 -> /SiPM_Connector(7-9)/BCH0
- J703 pad 20: GND -> /SiPM_Connector(7-9)/BCH9
- J703 pad 21: /SiPM_Connector(7-9)/BCH23 -> GND
- J703 pad 22: GND -> /SiPM_Connector(7-9)/BCH10
- J703 pad 23: /SiPM_Connector(7-9)/BCH22 -> GND
- J703 pad 24: GND -> /SiPM_Connector(7-9)/BCH11
- J703 pad 25: /SiPM_Connector(7-9)/BCH21 -> GND
- J703 pad 26: GND -> /SiPM_Connector(7-9)/BCH12
- J703 pad 27: /SiPM_Connector(7-9)/BCH20 -> GND
- J703 pad 28: GND -> /SiPM_Connector(7-9)/BCH13
- J703 pad 29: /SiPM_Connector(7-9)/BCH19 -> GND
- J703 pad 3: Net-(J703-Pad3) -> GND
- J703 pad 30: GND -> /SiPM_Connector(7-9)/BCH14
- J703 pad 31: /SiPM_Connector(7-9)/BCH18 -> GND
- J703 pad 32: GND -> /SiPM_Connector(7-9)/BCH15
- J703 pad 33: /SiPM_Connector(7-9)/BCH17 -> GND
- J703 pad 34: GND -> /SiPM_Connector(7-9)/BCH16
- J703 pad 35: /SiPM_Connector(7-9)/BCH16 -> GND
- J703 pad 36: GND -> /SiPM_Connector(7-9)/BCH17
- J703 pad 37: /SiPM_Connector(7-9)/BCH15 -> GND
- J703 pad 38: GND -> /SiPM_Connector(7-9)/BCH18
- J703 pad 39: /SiPM_Connector(7-9)/BCH14 -> GND
- J703 pad 4: GND -> /SiPM_Connector(7-9)/BCH1
- J703 pad 40: GND -> /SiPM_Connector(7-9)/BCH19
- J703 pad 41: /SiPM_Connector(7-9)/BCH13 -> GND
- J703 pad 42: GND -> /SiPM_Connector(7-9)/BCH20
- J703 pad 43: /SiPM_Connector(7-9)/BCH12 -> GND
- J703 pad 44: GND -> /SiPM_Connector(7-9)/BCH21
- J703 pad 45: /SiPM_Connector(7-9)/BCH11 -> GND
- J703 pad 46: GND -> /SiPM_Connector(7-9)/BCH22
- J703 pad 47: /SiPM_Connector(7-9)/BCH10 -> GND
- J703 pad 48: GND -> /SiPM_Connector(7-9)/BCH23
- J703 pad 49: /SiPM_Connector(7-9)/BCH9 -> GND
- J703 pad 5: /SiPM_Connector(7-9)/BCH31 -> GND
- J703 pad 50: GND -> /SiPM_Connector(7-9)/BCH24
- J703 pad 51: /SiPM_Connector(7-9)/BCH8 -> GND
- J703 pad 52: GND -> /SiPM_Connector(7-9)/BCH25
- J703 pad 53: /SiPM_Connector(7-9)/BCH7 -> GND
- J703 pad 54: GND -> /SiPM_Connector(7-9)/BCH26
- J703 pad 55: /SiPM_Connector(7-9)/BCH6 -> GND
- J703 pad 56: GND -> /SiPM_Connector(7-9)/BCH27
- J703 pad 57: /SiPM_Connector(7-9)/BCH5 -> GND
- J703 pad 58: GND -> /SiPM_Connector(7-9)/BCH28
- J703 pad 59: /SiPM_Connector(7-9)/BCH4 -> GND
- J703 pad 6: GND -> /SiPM_Connector(7-9)/BCH2
- J703 pad 60: GND -> /SiPM_Connector(7-9)/BCH29
- J703 pad 61: /SiPM_Connector(7-9)/BCH3 -> GND
- J703 pad 62: GND -> /SiPM_Connector(7-9)/BCH30
- J703 pad 63: /SiPM_Connector(7-9)/BCH2 -> GND
- J703 pad 64: GND -> /SiPM_Connector(7-9)/BCH31
- J703 pad 65: /SiPM_Connector(7-9)/BCH1 -> GND
- J703 pad 66: GND -> Net-(J703-Pad66)
- J703 pad 67: /SiPM_Connector(7-9)/BCH0 -> /SiPM_Connector(7-9)/BIAS4
- J703 pad 68: /SiPM_Connector(7-9)/BIAS3 -> Net-(J703-Pad68)
- J703 pad 7: /SiPM_Connector(7-9)/BCH30 -> GND
- J703 pad 8: GND -> /SiPM_Connector(7-9)/BCH3
- J703 pad 9: /SiPM_Connector(7-9)/BCH29 -> GND
- J803 pad 1: Net-(J803-Pad1) -> /SiPM_Connector(7-9)/BIAS3
- J803 pad 10: GND -> /SiPM_Connector(7-9)/BCH36
- J803 pad 11: /SiPM_Connector(7-9)/BCH60 -> GND
- J803 pad 12: GND -> /SiPM_Connector(7-9)/BCH37
- J803 pad 13: /SiPM_Connector(7-9)/BCH59 -> GND
- J803 pad 14: GND -> /SiPM_Connector(7-9)/BCH38
- J803 pad 15: /SiPM_Connector(7-9)/BCH58 -> GND
- J803 pad 16: GND -> /SiPM_Connector(7-9)/BCH39
- J803 pad 17: /SiPM_Connector(7-9)/BCH57 -> GND
- J803 pad 18: GND -> /SiPM_Connector(7-9)/BCH40
- J803 pad 19: /SiPM_Connector(7-9)/BCH56 -> GND
- J803 pad 2: /SiPM_Connector(7-9)/BIAS4 -> /SiPM_Connector(7-9)/BCH32
- J803 pad 20: GND -> /SiPM_Connector(7-9)/BCH41
- J803 pad 21: /SiPM_Connector(7-9)/BCH55 -> GND
- J803 pad 22: GND -> /SiPM_Connector(7-9)/BCH42
- J803 pad 23: /SiPM_Connector(7-9)/BCH54 -> GND
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
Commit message: Edited Backplane
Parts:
- moved J101 0.25 mm to (12.2, 25.0)
- moved J103 0.25 mm to (37.8, 25.0)
- moved J201 0.25 mm to (12.2, 76.0)
- moved J203 0.25 mm to (37.8, 76.0)
- moved J301 0.25 mm to (12.2, 127.0)
- moved J303 0.25 mm to (37.8, 127.0)
- moved J401 0.25 mm to (12.2, 178.0)
- moved J403 0.25 mm to (37.8, 178.0)
- moved J501 0.25 mm to (12.2, 229.0)
- moved J503 0.25 mm to (37.8, 229.0)
- moved J601 0.25 mm to (12.2, 280.0)
- moved J603 0.25 mm to (37.8, 280.0)
- moved J701 0.25 mm to (12.2, 331.0)
- moved J703 0.25 mm to (37.8, 331.0)
- moved J801 0.25 mm to (12.2, 382.0)
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- renumbered J702 to J1, J902 to J2
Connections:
- J1 pad 75: /SiPM_Connector(7-9)/BIAS3 -> /SiPM_Connector(7-9)/BIAS27
- J1 pad 76: /SiPM_Connector(7-9)/BIAS1 -> /SiPM_Connector(7-9)/BIAS25
- J1 pad 79: /SiPM_Connector(7-9)/BIAS4 -> /SiPM_Connector(7-9)/BIAS28
- J1 pad 80: /SiPM_Connector(7-9)/BIAS2 -> /SiPM_Connector(7-9)/BIAS26
- J2 pad 115: /SiPM_Connector(7-9)/BIAS3 -> /SiPM_Connector(7-9)/BIAS35
- J2 pad 116: /SiPM_Connector(7-9)/BIAS1 -> /SiPM_Connector(7-9)/BIAS33
- J2 pad 119: /SiPM_Connector(7-9)/BIAS4 -> /SiPM_Connector(7-9)/BIAS36
- J2 pad 120: /SiPM_Connector(7-9)/BIAS2 -> /SiPM_Connector(7-9)/BIAS34
- J2 pad 35: /SiPM_Connector(7-9)/BIAS3 -> /SiPM_Connector(7-9)/BIAS31
- J2 pad 36: /SiPM_Connector(7-9)/BIAS1 -> /SiPM_Connector(7-9)/BIAS29
- J2 pad 39: /SiPM_Connector(7-9)/BIAS4 -> /SiPM_Connector(7-9)/BIAS32
- J2 pad 40: /SiPM_Connector(7-9)/BIAS2 -> /SiPM_Connector(7-9)/BIAS30
- J201 pad 2: /SiPM_Connector(1-3)/BIAS1 -> /SiPM_Connector(1-3)/BIAS5
- J201 pad 68: /SiPM_Connector(1-3)/BIAS2 -> /SiPM_Connector(1-3)/BIAS6
- J203 pad 1: /SiPM_Connector(1-3)/BIAS3 -> /SiPM_Connector(1-3)/BIAS7
- J203 pad 67: /SiPM_Connector(1-3)/BIAS4 -> /SiPM_Connector(1-3)/BIAS8
- J301 pad 2: /SiPM_Connector(1-3)/BIAS1 -> /SiPM_Connector(1-3)/BIAS9
- J301 pad 68: /SiPM_Connector(1-3)/BIAS2 -> /SiPM_Connector(1-3)/BIAS10
- J302 pad 115: /SiPM_Connector(1-3)/BIAS3 -> /SiPM_Connector(1-3)/BIAS11
- J302 pad 116: /SiPM_Connector(1-3)/BIAS1 -> /SiPM_Connector(1-3)/BIAS9
- J302 pad 119: /SiPM_Connector(1-3)/BIAS4 -> /SiPM_Connector(1-3)/BIAS12
- J302 pad 120: /SiPM_Connector(1-3)/BIAS2 -> /SiPM_Connector(1-3)/BIAS10
- J302 pad 35: /SiPM_Connector(1-3)/BIAS3 -> /SiPM_Connector(1-3)/BIAS7
- J302 pad 36: /SiPM_Connector(1-3)/BIAS1 -> /SiPM_Connector(1-3)/BIAS5
- J302 pad 39: /SiPM_Connector(1-3)/BIAS4 -> /SiPM_Connector(1-3)/BIAS8
- J302 pad 40: /SiPM_Connector(1-3)/BIAS2 -> /SiPM_Connector(1-3)/BIAS6
- J303 pad 1: /SiPM_Connector(1-3)/BIAS3 -> /SiPM_Connector(1-3)/BIAS11
- J303 pad 67: /SiPM_Connector(1-3)/BIAS4 -> /SiPM_Connector(1-3)/BIAS12
- J401 pad 2: /SiPM_Connector(4-6)/BIAS1 -> /SiPM_Connector(4-6)/BIAS13
- J401 pad 68: /SiPM_Connector(4-6)/BIAS2 -> /SiPM_Connector(4-6)/BIAS14
- J402 pad 75: /SiPM_Connector(4-6)/BIAS3 -> /SiPM_Connector(4-6)/BIAS15
- J402 pad 76: /SiPM_Connector(4-6)/BIAS1 -> /SiPM_Connector(4-6)/BIAS13
- J402 pad 79: /SiPM_Connector(4-6)/BIAS4 -> /SiPM_Connector(4-6)/BIAS16
- J402 pad 80: /SiPM_Connector(4-6)/BIAS2 -> /SiPM_Connector(4-6)/BIAS14
- J403 pad 1: /SiPM_Connector(4-6)/BIAS3 -> /SiPM_Connector(4-6)/BIAS15
- J403 pad 67: /SiPM_Connector(4-6)/BIAS4 -> /SiPM_Connector(4-6)/BIAS16
- J501 pad 2: /SiPM_Connector(4-6)/BIAS1 -> /SiPM_Connector(4-6)/BIAS17
- J501 pad 68: /SiPM_Connector(4-6)/BIAS2 -> /SiPM_Connector(4-6)/BIAS18
- J503 pad 1: /SiPM_Connector(4-6)/BIAS3 -> /SiPM_Connector(4-6)/BIAS19
- J503 pad 67: /SiPM_Connector(4-6)/BIAS4 -> /SiPM_Connector(4-6)/BIAS20
- J601 pad 2: /SiPM_Connector(4-6)/BIAS1 -> /SiPM_Connector(4-6)/BIAS21
- J601 pad 68: /SiPM_Connector(4-6)/BIAS2 -> /SiPM_Connector(4-6)/BIAS22
- J602 pad 115: /SiPM_Connector(4-6)/BIAS3 -> /SiPM_Connector(4-6)/BIAS23
- J602 pad 116: /SiPM_Connector(4-6)/BIAS1 -> /SiPM_Connector(4-6)/BIAS21
- J602 pad 119: /SiPM_Connector(4-6)/BIAS4 -> /SiPM_Connector(4-6)/BIAS24
- J602 pad 120: /SiPM_Connector(4-6)/BIAS2 -> /SiPM_Connector(4-6)/BIAS22
- J602 pad 35: /SiPM_Connector(4-6)/BIAS3 -> /SiPM_Connector(4-6)/BIAS19
- J602 pad 36: /SiPM_Connector(4-6)/BIAS1 -> /SiPM_Connector(4-6)/BIAS17
- J602 pad 39: /SiPM_Connector(4-6)/BIAS4 -> /SiPM_Connector(4-6)/BIAS20
- J602 pad 40: /SiPM_Connector(4-6)/BIAS2 -> /SiPM_Connector(4-6)/BIAS18
- J603 pad 1: /SiPM_Connector(4-6)/BIAS3 -> /SiPM_Connector(4-6)/BIAS23
- J603 pad 67: /SiPM_Connector(4-6)/BIAS4 -> /SiPM_Connector(4-6)/BIAS24
- J701 pad 2: /SiPM_Connector(7-9)/BIAS1 -> /SiPM_Connector(7-9)/BIAS25
- J701 pad 68: /SiPM_Connector(7-9)/BIAS2 -> /SiPM_Connector(7-9)/BIAS26
- J703 pad 1: /SiPM_Connector(7-9)/BIAS3 -> /SiPM_Connector(7-9)/BIAS27
- J703 pad 67: /SiPM_Connector(7-9)/BIAS4 -> /SiPM_Connector(7-9)/BIAS28
- J801 pad 2: /SiPM_Connector(7-9)/BIAS1 -> /SiPM_Connector(7-9)/BIAS29
- J801 pad 68: /SiPM_Connector(7-9)/BIAS2 -> /SiPM_Connector(7-9)/BIAS30
- J803 pad 1: /SiPM_Connector(7-9)/BIAS3 -> /SiPM_Connector(7-9)/BIAS31
- J803 pad 67: /SiPM_Connector(7-9)/BIAS4 -> /SiPM_Connector(7-9)/BIAS32
- J901 pad 2: /SiPM_Connector(7-9)/BIAS1 -> /SiPM_Connector(7-9)/BIAS33
- J901 pad 68: /SiPM_Connector(7-9)/BIAS2 -> /SiPM_Connector(7-9)/BIAS34
- J903 pad 1: /SiPM_Connector(7-9)/BIAS3 -> /SiPM_Connector(7-9)/BIAS35
- J903 pad 67: /SiPM_Connector(7-9)/BIAS4 -> /SiPM_Connector(7-9)/BIAS36
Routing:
- net /SiPM_Connector(1-3)/BIAS1: track 161.3 -> 46.7 mm, vias 3 -> 1
- net /SiPM_Connector(1-3)/BIAS3: track 161.3 -> 46.7 mm, vias 3 -> 1
- net /SiPM_Connector(1-3)/BIAS7: track 0.00 -> 61.5 mm, vias 0 -> 1
- net /SiPM_Connector(1-3)/BIAS5: track 0.00 -> 61.5 mm, vias 0 -> 1
- net /SiPM_Connector(1-3)/BIAS11: track 0.00 -> 53.0 mm, vias 0 -> 1
- net /SiPM_Connector(1-3)/BIAS9: track 0.00 -> 53.0 mm, vias 0 -> 1
- net /SiPM_Connector(1-3)/BIAS4: track 63.8 -> 15.9 mm, vias 3 -> 1
- net /SiPM_Connector(1-3)/BIAS2: track 63.8 -> 15.9 mm, vias 3 -> 1
- net /SiPM_Connector(1-3)/BIAS6: track 0.00 -> 25.2 mm, vias 0 -> 1
- net /SiPM_Connector(1-3)/BIAS8: track 0.00 -> 25.2 mm, vias 0 -> 1
- net /SiPM_Connector(1-3)/BIAS12: track 0.00 -> 22.7 mm, vias 0 -> 1
- net /SiPM_Connector(1-3)/BIAS10: track 0.00 -> 22.7 mm, vias 0 -> 1

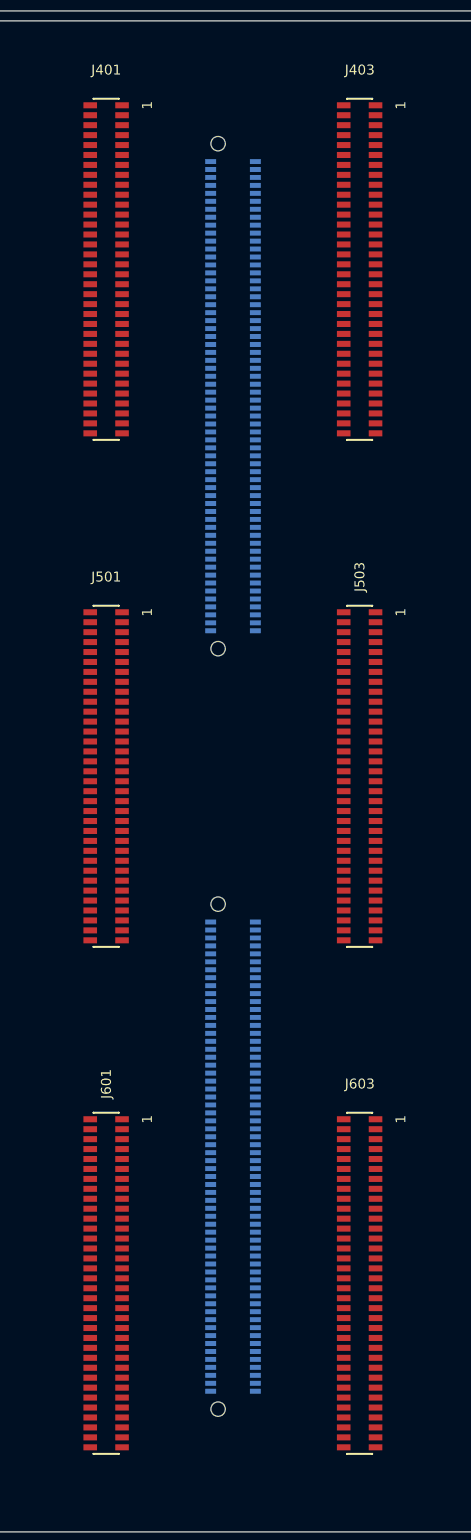
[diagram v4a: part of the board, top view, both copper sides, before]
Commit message: Backplane Layout edited
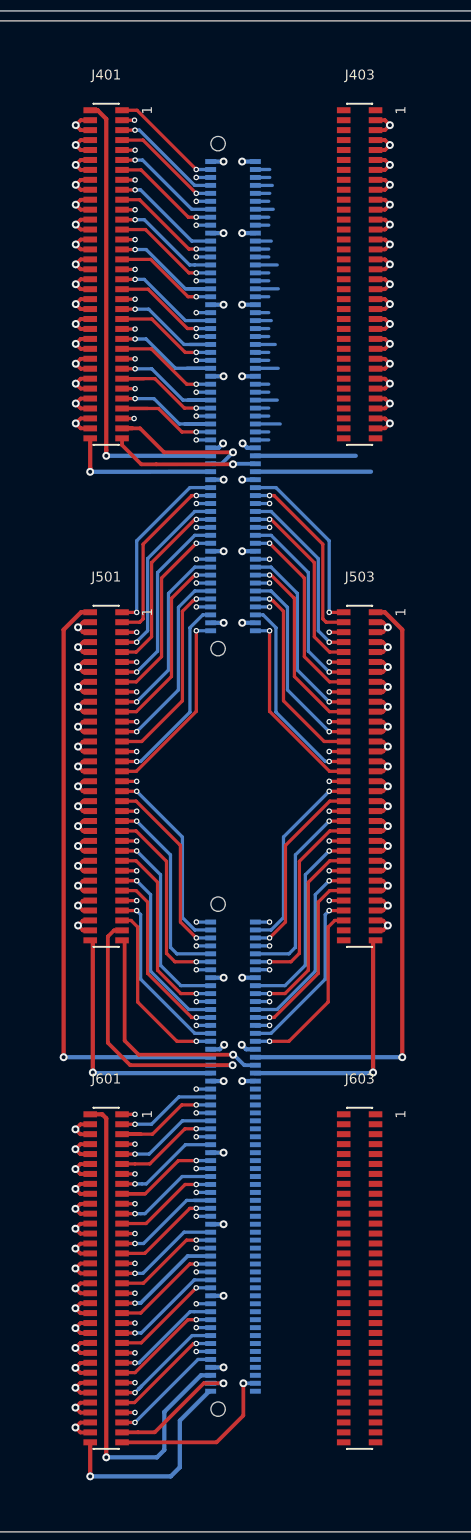
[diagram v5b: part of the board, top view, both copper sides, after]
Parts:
- moved J401 0.50 mm to (12.2, 178.5)
- moved J403 0.50 mm to (37.8, 178.5)
- moved J601 0.50 mm to (12.2, 279.5)
- moved J603 0.50 mm to (37.8, 279.5)
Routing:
- net GND: track 476.0 -> 775.3 mm, vias 168 -> 274
- net /SiPM_Connector(4-6)/BIAS17: track 0.00 -> 61.5 mm, vias 0 -> 1
- net /SiPM_Connector(4-6)/BIAS19: track 0.00 -> 61.5 mm, vias 0 -> 1
- net /SiPM_Connector(4-6)/VDD: track 0.00 -> 57.8 mm, vias 0 -> 3
- net /SiPM_Connector(4-6)/OUT: track 0.00 -> 57.0 mm, vias 0 -> 3
- net /SiPM_Connector(4-6)/BIAS21: track 0.00 -> 52.0 mm, vias 0 -> 1
- net /SiPM_Connector(4-6)/BIAS13: track 0.00 -> 46.4 mm, vias 0 -> 1
- net /SiPM_Connector(4-6)/BIAS18: track 0.00 -> 25.2 mm, vias 0 -> 1
- net /SiPM_Connector(4-6)/BIAS20: track 0.00 -> 25.2 mm, vias 0 -> 1
- net /SiPM_Connector(4-6)/BIAS22: track 0.00 -> 21.8 mm, vias 0 -> 1
- net /SiPM_Connector(4-6)/CH46: track 0.00 -> 20.3 mm, vias 0 -> 2
- net /SiPM_Connector(4-6)/BCH46: track 0.00 -> 20.3 mm, vias 0 -> 2
- net /SiPM_Connector(4-6)/CH45: track 0.00 -> 20.0 mm, vias 0 -> 1
- net /SiPM_Connector(4-6)/BCH45: track 0.00 -> 20.0 mm, vias 0 -> 1
- net /SiPM_Connector(4-6)/CH47: track 0.00 -> 19.8 mm, vias 0 -> 1
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
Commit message: Backplane Layout Edited
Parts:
- moved J101 0.50 mm to (12.2, 25.5)
- moved J103 0.50 mm to (37.8, 25.5)
- moved J301 0.50 mm to (12.2, 126.5)
- moved J303 0.50 mm to (37.8, 126.5)
- moved J701 0.50 mm to (12.2, 331.5)
- moved J703 0.50 mm to (37.8, 331.5)
- moved J901 0.50 mm to (12.2, 432.5)
- moved J903 0.50 mm to (37.8, 432.5)
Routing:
- net GND: track 775.3 -> 1194.9 mm, vias 274 -> 420
- net /SiPM_Connector(7-9)/BIAS29: track 0.00 -> 61.5 mm, vias 0 -> 1
- net /SiPM_Connector(7-9)/BIAS31: track 0.00 -> 61.5 mm, vias 0 -> 1
- net /SiPM_Connector(7-9)/VDD: track 0.00 -> 57.8 mm, vias 0 -> 3
- net /SiPM_Connector(7-9)/OUT: track 0.00 -> 57.0 mm, vias 0 -> 3
- net /SiPM_Connector(7-9)/BIAS35: track 0.00 -> 52.0 mm, vias 0 -> 1
- net /SiPM_Connector(7-9)/BIAS33: track 0.00 -> 52.0 mm, vias 0 -> 1
- net /SiPM_Connector(4-6)/BIAS23: track 0.00 -> 52.0 mm, vias 0 -> 1
- net /SiPM_Connector(7-9)/BIAS27: track 0.00 -> 46.4 mm, vias 0 -> 1
- net /SiPM_Connector(7-9)/BIAS25: track 0.00 -> 46.4 mm, vias 0 -> 1
- net /SiPM_Connector(4-6)/BIAS15: track 10.2 -> 46.4 mm, vias 0 -> 1
- net /SiPM_Connector(7-9)/BIAS32: track 0.00 -> 25.2 mm, vias 0 -> 1
- net /SiPM_Connector(7-9)/BIAS30: track 0.00 -> 25.2 mm, vias 0 -> 1
- net /SiPM_Connector(7-9)/BIAS36: track 0.00 -> 21.8 mm, vias 0 -> 1
- net /SiPM_Connector(7-9)/BIAS34: track 0.00 -> 21.8 mm, vias 0 -> 1
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
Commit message: Backplane Layout Edited
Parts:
- removed H1, H2, H3, H4: MountingHole, MountingHole:MountingHole_4.3mm_M4_Pad
- removed the J1 at (-55.9, 79.9)
- removed the J2 at (-43.4, 79.9)
- removed J3: Conn_02x34_Odd_Even, Backplane-prototype:SAMTEC_CLM-134-02-F-D
- moved J2 3.75 mm to (25.0, 416.5)
- moved J1 3.00 mm to (25.0, 340.8)
- moved J701 3.00 mm to (12.2, 328.5)
- moved J703 3.00 mm to (37.8, 328.5)
- moved J801 3.00 mm to (12.2, 379.0)
- moved J803 3.00 mm to (37.8, 379.0)
- moved J901 3.00 mm to (12.2, 429.5)
- moved J903 3.00 mm to (37.8, 429.5)
- moved J602 2.25 mm to (25.0, 265.0)
- moved J401 1.50 mm to (12.2, 177.0)
- moved J402 1.50 mm to (25.0, 189.2)
- moved J403 1.50 mm to (37.8, 177.0)
- moved J501 1.50 mm to (12.2, 227.5)
- moved J503 1.50 mm to (37.8, 227.5)
- moved J601 1.50 mm to (12.2, 278.0)
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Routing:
- net GND: track 1194.9 -> 1029.8 mm, vias 420 -> 343
- net /BIAS3: track 51.4 -> 0.00 mm, vias 1 -> 0
- net /BIAS1: track 51.4 -> 0.00 mm, vias 1 -> 0
- net /SiPM_Connector(4-6)/OUT: track 57.0 -> 24.5 mm, vias 3 -> 2
- net /SiPM_Connector(4-6)/VDD: track 57.8 -> 32.0 mm
- net /OUT: track 22.5 -> 0.00 mm, vias 1 -> 0
- net /BIAS4: track 20.1 -> 0.00 mm, vias 1 -> 0
- net /BIAS2: track 20.1 -> 0.00 mm, vias 1 -> 0
- net /SiPM_Connector(4-6)/BCH53: track 19.7 -> 0.00 mm, vias 1 -> 0
- net /SiPM_Connector(4-6)/BCH56: track 19.7 -> 0.00 mm, vias 1 -> 0
- net /SiPM_Connector(4-6)/BCH52: track 19.6 -> 0.00 mm, vias 2 -> 0
- net /SiPM_Connector(4-6)/BCH55: track 19.6 -> 0.00 mm, vias 2 -> 0
- net /SiPM_Connector(4-6)/BCH54: track 19.5 -> 0.00 mm, vias 1 -> 0
- net /SiPM_Connector(4-6)/BCH49: track 19.4 -> 0.00 mm, vias 2 -> 0
- net /SiPM_Connector(4-6)/BCH57: track 19.4 -> 0.00 mm, vias 1 -> 0
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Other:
- board size 123.4 x 458 mm -> 50 x 455 mm
- board text removed: "Backplane prototype kept here for reference"
- board text removed: "EMPHATIC Backplane Prototype REV C"
- board text removed: "S/N:"
- board text removed: "T.Agarwal - 2021 - 05"
- board text removed: "http://edf.bu.edu"
